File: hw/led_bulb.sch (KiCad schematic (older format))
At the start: 93 parts, among them P1 USB_OTG, P10 CONN_01X04, P11 CONN_01X04, P12 CONN_01X04, P13 CONN_01X04, P14 CONN_01X04, P15 CONN_01X04, P16 CONN_01X04, P17 CONN_01X04, P2 CONN_01X04, P3 CONN_01X04, P4 CONN_01X04, P5 CONN_01X04, P6 CONN_01X04, P7 CONN_01X04, P8 CONN_01X04, P9 CONN_01X04, SW1 SW_RST, SW2 SW_FLASH, U1 CP2102, U3 ESP-12E, U4 AP1117D33

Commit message: Added first version of v4 hardware.
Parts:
- removed P10, P11, P12, P13, P14, P15, P16, P17, P2, P3, P4, P5, P6, P7, P8, P9: CONN_01X04, Connectors:CONN_2.54mm_1x4, symbol CONN_01X04
- removed R6: 470, Resistors_SMD:R_0603, symbol R-RESCUE-led_matrix_apa102
- added P10, P11, P12, P13, P14, P15, P16, P17, P18, P19, P2, P20, P21, P22, P23, P24, P25, P26, P27, P28, P29, P3, P30, P31, P32, P33, P4, P5, P6, P7, P8, P9: CONN_01X02, footprints:CONN_2.54mm_1x2_no-outline, symbol CONN_01X02
- added R6: 470, Resistors_SMD:R_0603, symbol R_Small
- D1: footprint LEDs:LED-0603 -> Capacitors_SMD:C_0603
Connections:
- net labels removed: DTR, RTS
- wire segments 365 -> 363
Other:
- moved on the sheet: C10, C2, C3, C4, C5, C6, C7, C8, LED1, LED10, LED11, LED12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

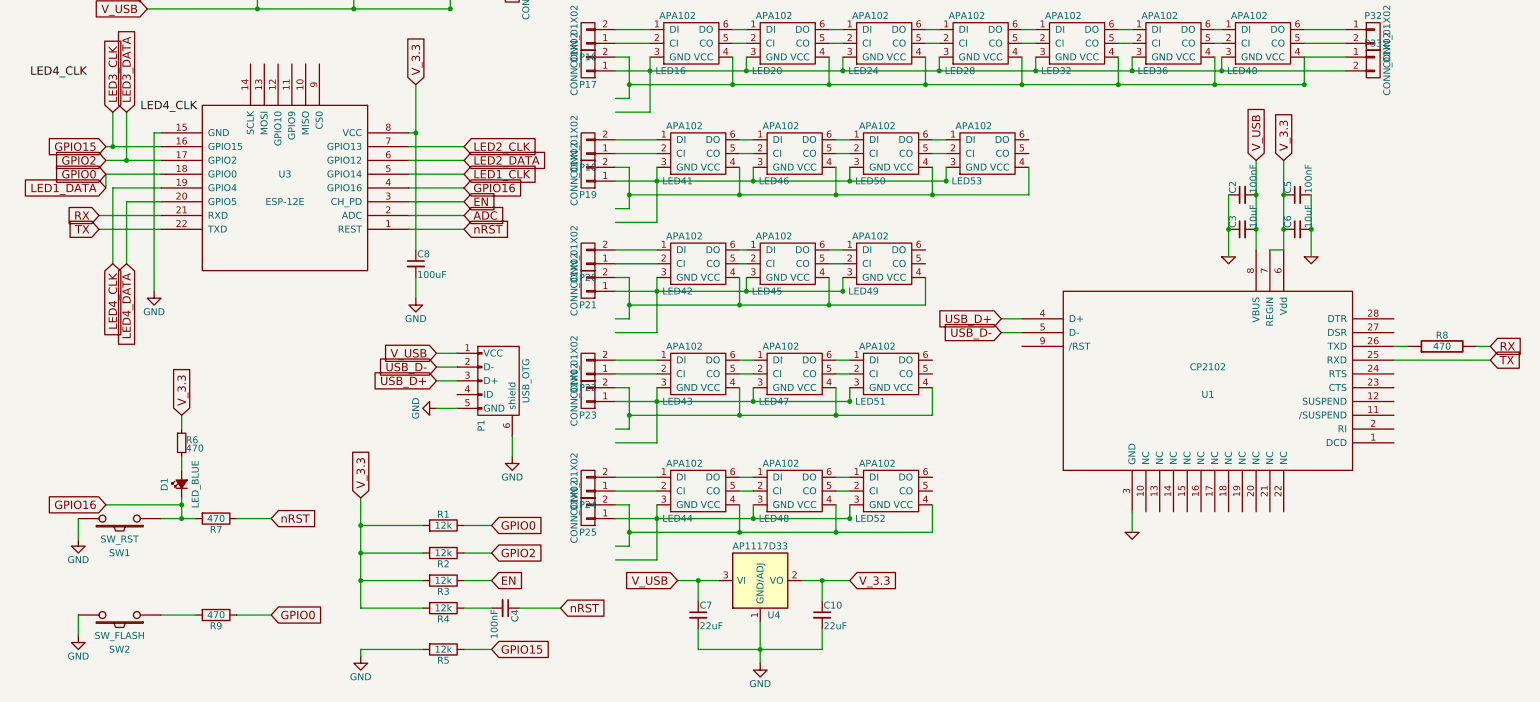
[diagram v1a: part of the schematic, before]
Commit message: Added transistor to allow automatic flashing.
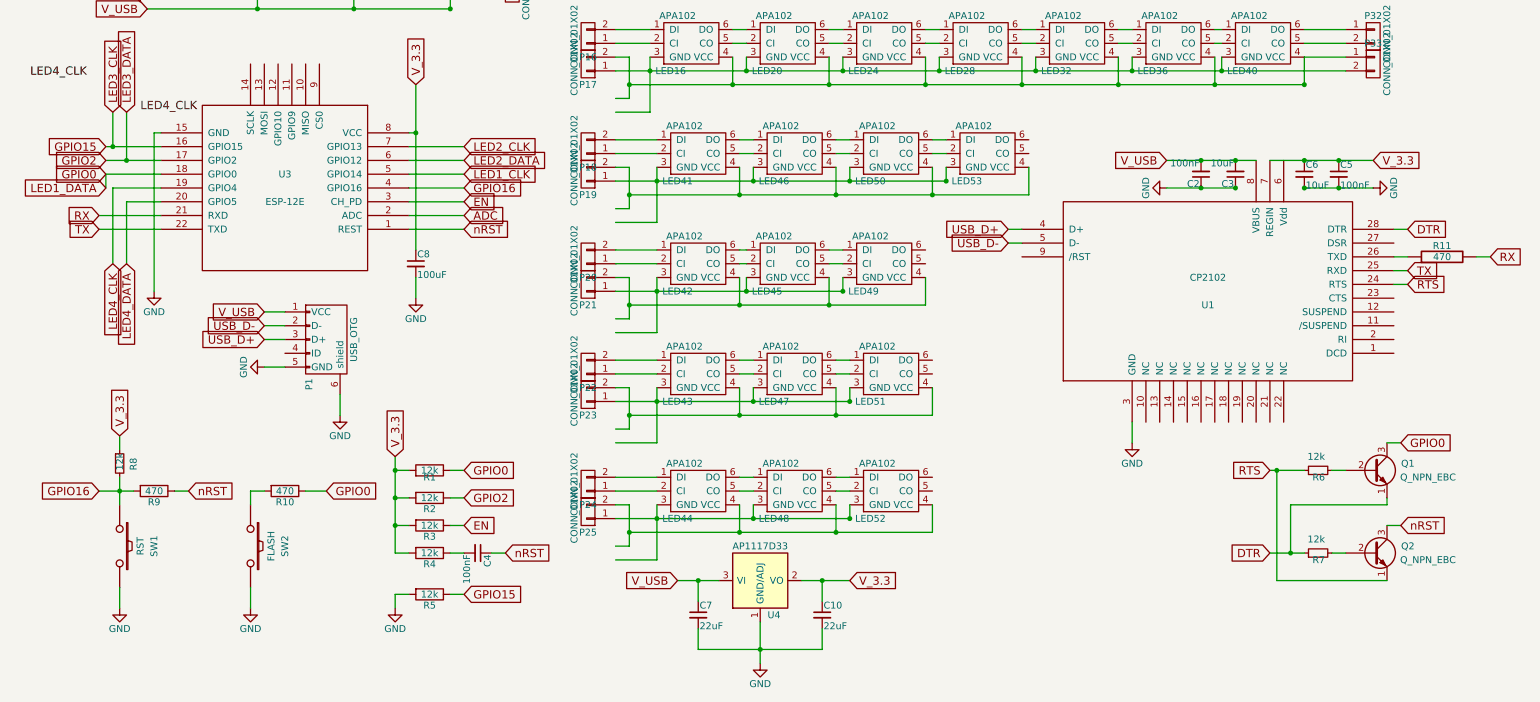
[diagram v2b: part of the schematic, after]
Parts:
- removed D1: LED_BLUE, Capacitors_SMD:C_0603, symbol Led_Small
- added Q1, Q2: Q_NPN_EBC, TO_SOT_Packages_SMD:SOT-23, symbol Q_NPN_EBC
- added R7, R8: 12k, Resistors_SMD:R_0603, symbol R_Small
- R6: value 470 -> 12k
- SW1: value SW_RST -> RST
- SW2: value SW_FLASH -> FLASH
- renumbered R9 to R10, R8 to R11, R7 to R9
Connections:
- net labels added: DTR, RTS
- wire segments 363 -> 374
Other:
- moved on the sheet: C2, C3, C4, C5, C6, P1, R1, R10, R11, R2, R3, R4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
